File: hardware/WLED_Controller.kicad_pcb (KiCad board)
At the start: 2 copper layers, 50 x 57.5 mm, 79 parts, among them J1 Conn_01x01_Male, J11 Conn_01x01_Male, J12 Conn_01x01_Male, J2 USB_B_Micro, J3 Conn_01x01_Male, J4 Conn_01x01_Male, J5 Conn_01x01_Male, Q1 S8050_SMD, Q2 S8050_SMD, Q3 2N7002, Q4 2N7002, SW1 SW_SPST, SW2 SW_SPST, U1 AMS1117-3.3, U2 AMS1117-3.3, U3 TP4056, U4 ESP-12F, U5 CP2102N-A01-GQFN28, U6 AP2007, U7 AP2007, U8 AP2007

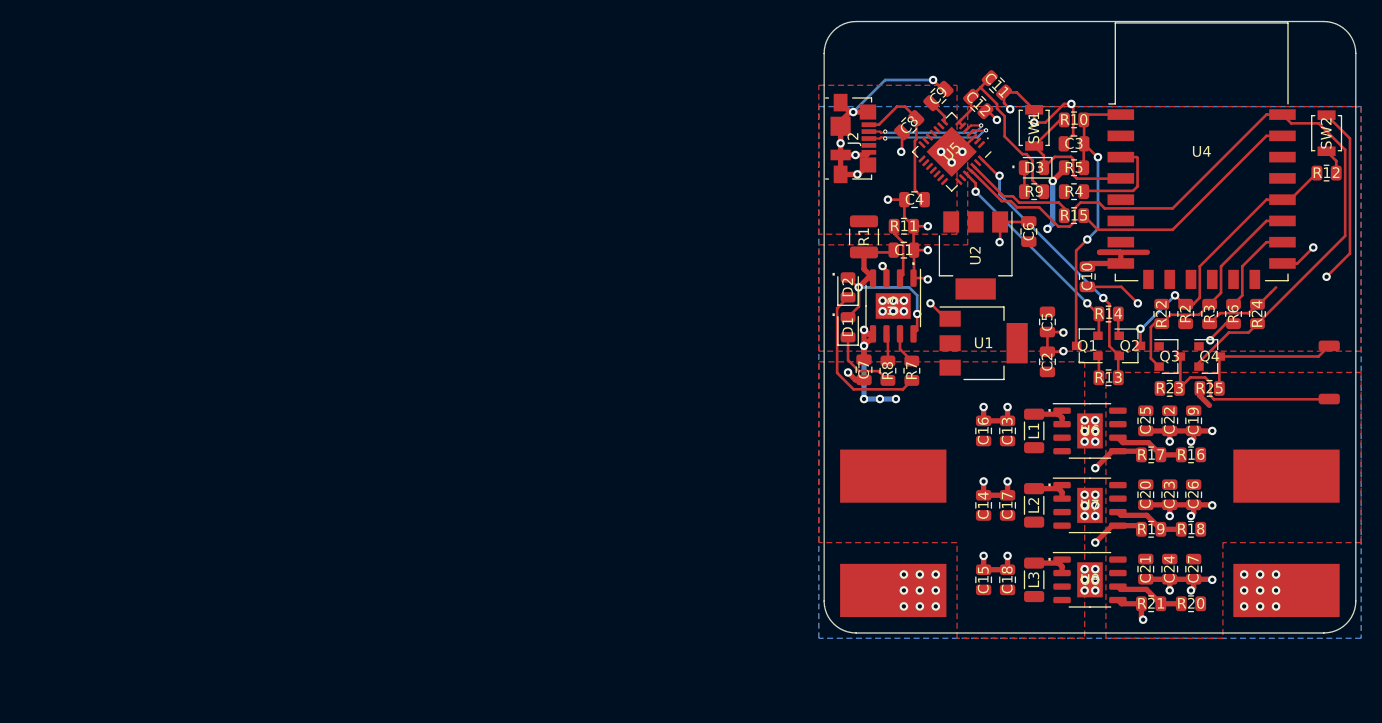
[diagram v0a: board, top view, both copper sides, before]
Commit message: Updated to v2.0.0
Contains the PCB design and fabrication files for v2.0.0 of the WLED
controller.
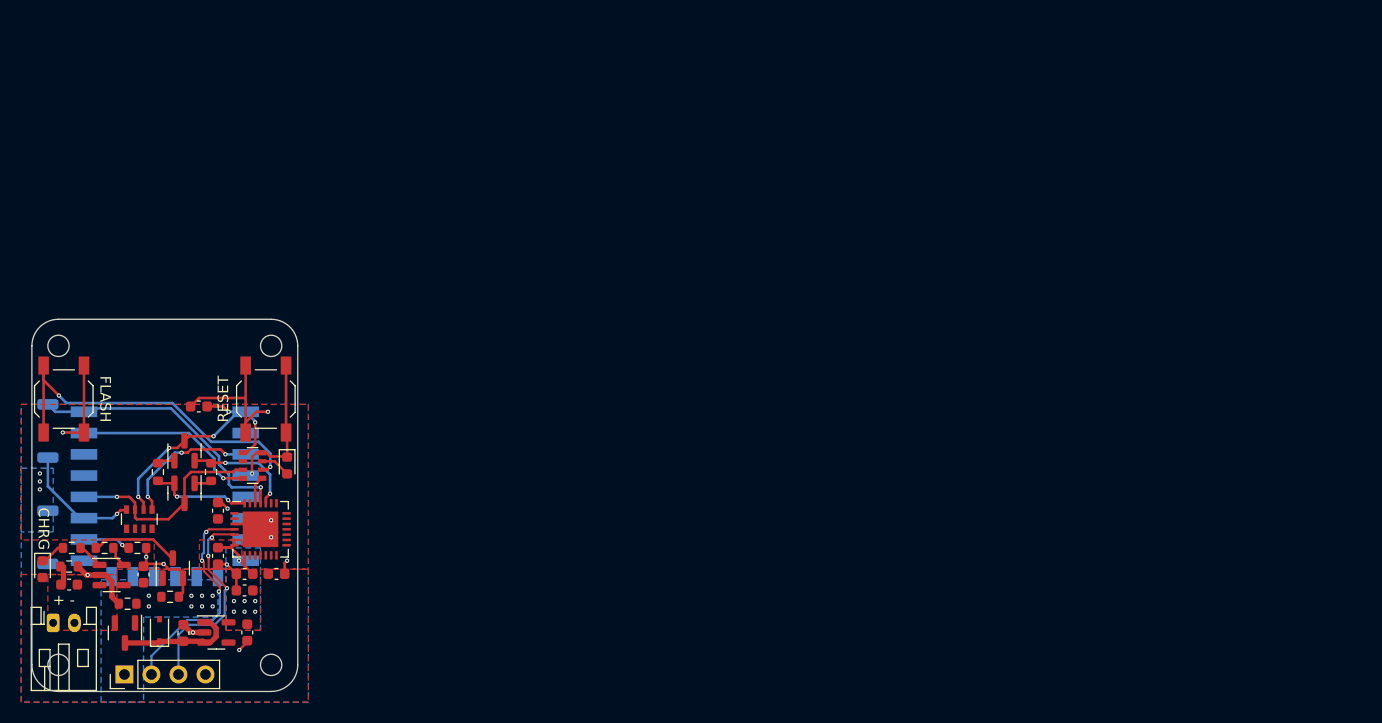
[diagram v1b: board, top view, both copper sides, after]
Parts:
- removed C11: 10uF, Capacitor_SMD:C_0805_2012Metric
- removed C12: 0.1uF, Capacitor_SMD:C_0805_2012Metric
- removed C13, C14, C15, C16, C17, C18, C19, C20, C21, C22, C23, C24, C25, C26, C27: 22u, Capacitor_SMD:C_0805_2012Metric
- removed J11, J12: Conn_01x01_Male, Connector_Wire:SolderWirePad_1x01_SMD_1x2mm
- removed L1, L2, L3: 3.3u, Inductor_SMD:L_1206_3216Metric
- removed R10, R12, R15, R9: 470, Resistor_SMD:R_0805_2012Metric
- removed R11: 1.2k, Resistor_SMD:R_0805_2012Metric
- removed R13, R14, R22, R23, R24, R25: 10k, Resistor_SMD:R_0805_2012Metric
- removed R16, R18, R20: 100k, Resistor_SMD:R_0805_2012Metric
- removed R17, R19, R21: 33k, Resistor_SMD:R_0805_2012Metric
- removed U5: CP2102N-A01-GQFN28, Package_DFN_QFN:QFN-28-1EP_5x5mm_P0.5mm_EP3.35x3.35mm
- removed U6, U7, U8: AP2007, myfootprints:SOP-8-EP_3.9x4.9mm_P1.27mm
- added J6: Conn_01x01_Male, Connector_Wire:SolderWirePad_1x01_SMD_1x2mm, B.Cu at (51.5, 118.0)
- added RN1: 10k, Resistor_SMD:R_Array_Convex_4x0603, F.Cu at (60.1, 113.8)
- added RN2: 470, Resistor_SMD:R_Array_Convex_4x0603, F.Cu at (70.8, 108.8)
- added kibuzzard-6350B1D2: G***, kibuzzard-6350B1D2, B.Cu at (62.5, 122.9)
- C1, C6, C8: value 10uF -> 0.1uF; footprint Capacitor_SMD:C_0805_2012Metric -> Capacitor_SMD:C_0603_1608Metric
- C10, C7: footprint Capacitor_SMD:C_0805_2012Metric -> Capacitor_SMD:C_0603_1608Metric
- C2, C4, C5: value 10uF -> 1uF; footprint Capacitor_SMD:C_0805_2012Metric -> Capacitor_SMD:C_0603_1608Metric
- C3: value 0.1uF -> 1uF; footprint Capacitor_SMD:C_0805_2012Metric -> Capacitor_SMD:C_0603_1608Metric
- C9: value 0.1uF -> 10uF; footprint Capacitor_SMD:C_0805_2012Metric -> Capacitor_SMD:C_0603_1608Metric
- D1: value LED -> 1N5819; footprint LED_SMD:LED_0805_2012Metric -> Diode_SMD:D_SOD-323
- D2, D3: footprint LED_SMD:LED_0805_2012Metric -> LED_SMD:LED_0603_1608Metric
- J1: value Conn_01x01_Male -> Conn_01x02_Male; footprint Connector_Wire:SolderWirePad_1x01_SMD_5x10mm -> Connector_JST:JST_PH_S2B-PH-K_1x02_P2.00mm_Horizontal
- J2: value USB_B_Micro -> Conn_01x04; footprint Connector_USB:USB_Micro-B_Molex_47346-0001 -> Connector_PinHeader_2.54mm:PinHeader_1x04_P2.54mm_Vertical
- J3, J4, J5: footprint Connector_Wire:SolderWirePad_1x01_SMD_5x10mm -> Connector_Wire:SolderWirePad_1x01_SMD_1x2mm; moved to B.Cu
- Q1: value S8050_SMD -> AO3401A
- Q2: value S8050_SMD -> AO3400A
- Q3, Q4: value 2N7002 -> AO3400A
- R1: value 0.4 -> 10k; footprint Resistor_SMD:R_1210_3225Metric -> Resistor_SMD:R_0603_1608Metric
- R2, R3: value 10k -> 100k; footprint Resistor_SMD:R_0805_2012Metric -> Resistor_SMD:R_0603_1608Metric
- R4: value 10k -> 330; footprint Resistor_SMD:R_0805_2012Metric -> Resistor_SMD:R_0603_1608Metric
- R5: value 10k -> 2k; footprint Resistor_SMD:R_0805_2012Metric -> Resistor_SMD:R_0603_1608Metric
- R6: value 10k -> 1; footprint Resistor_SMD:R_0805_2012Metric -> Resistor_SMD:R_0603_1608Metric
- R7, R8: value 1k -> 10k; footprint Resistor_SMD:R_0805_2012Metric -> Resistor_SMD:R_0603_1608Metric
- SW1, SW2: footprint Button_Switch_SMD:SW_SPST_B3U-1000P -> Button_Switch_SMD:SW_SPST_TL3342
- U1: value AMS1117-3.3 -> AP2112K-3.3; footprint Package_TO_SOT_SMD:SOT-223 -> Package_TO_SOT_SMD:SOT-23-5
- U2: value AMS1117-3.3 -> LTC4054ES5-4.2; footprint Package_TO_SOT_SMD:SOT-223 -> Package_TO_SOT_SMD:TSOT-23-5
- U3: value TP4056 -> ESP-12F; footprint myfootprints:SOP-8-EP_3.9x4.9mm_P1.27mm -> RF_Module:ESP-12E; moved to B.Cu
- U4: value ESP-12F -> CP2102N-Axx-xQFN28; footprint RF_Module:ESP-12E -> Package_DFN_QFN:QFN-28-1EP_5x5mm_P0.5mm_EP3.35x3.35mm
- moved SW2 121.4 mm to (53.0, 102.5)
- moved J5 117.8 mm to (51.5, 103.0), turned to 90 degrees
- moved J4 116.5 mm to (51.5, 108.0), turned to 90 degrees
- moved R6 112.0 mm to (53.5, 118.2), turned to 180 degrees
- moved R2 103.2 mm to (59.0, 121.8), turned to 180 degrees
- moved R3 101.3 mm to (63.0, 121.1), turned to 0 degrees
- moved D3 100.6 mm to (51.0, 118.5), turned to -90 degrees
- moved R4 100.0 mm to (53.8, 116.5), turned to 0 degrees
- moved R5 97.9 mm to (56.8, 116.5)
- moved Q4 97.3 mm to (64.3, 111.4), turned to -90 degrees
- moved U4 95.4 mm to (71.5, 114.8)
- moved C5 95.3 mm to (53.5, 120.0), turned to 0 degrees
- moved Q1 94.4 mm to (58.8, 124.5), turned to -90 degrees
- moved Q3 93.1 mm to (64.3, 107.4), turned to 90 degrees
- moved Q2 92.4 mm to (63.2, 118.4), turned to 90 degrees
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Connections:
- C1 pad 1: Net-(C1-Pad1) -> /nRST
- C10 pad 1: GND -> +3V3
- C10 pad 2: +3V3 -> GND
- C2 pad 1: +BATT -> Net-(C2-Pad1)
- C3 pad 1: /nRST -> +3V3
- C5 pad 1: +3V3 -> Net-(C5-Pad1)
- C5 pad 2: GND -> +BATT
- C6 pad 1: +3V3 -> GND
- C6 pad 2: GND -> +3V3
- C7 pad 1: +BATT -> VBUS
- C9 pad 1: VBUS -> +3V3
- D1 pad 1: Net-(D1-Pad1) -> Net-(C2-Pad1)
- D1 pad 2: Net-(C1-Pad1) -> VBUS
- D2 pad 1: Net-(D2-Pad1) -> /GPIO16
- D2 pad 2: Net-(C1-Pad1) -> Net-(D2-Pad2)
- D3 pad 1: /GPIO16 -> Net-(D3-Pad1)
- D3 pad 2: Net-(D3-Pad2) -> VBUS
- J2 pad 2: /D_N -> /D_P
- J2 pad 3: /D_P -> /D_N
- J2 pad 4: unconnected-(J2-Pad4) -> GND
- J3 pad 1: GND -> +3V3
- J4 pad 1: +5V -> /GPIO2
- J5 pad 1: GND -> /RXI
- Q1 pad 1: Net-(Q1-Pad1) -> VBUS
- Q1 pad 2: /RTS -> +BATT
- Q1 pad 3: /nRST -> Net-(C2-Pad1)
- Q2 pad 1: Net-(Q2-Pad1) -> VBUS
- Q2 pad 2: /DTR -> GND
- Q2 pad 3: /GPIO0 -> Net-(Q2-Pad3)
- Q3 pad 1: +3V3 -> Net-(Q3-Pad1)
- Q3 pad 2: /GPIO2 -> /RTS
- Q3 pad 3: /DATA -> /nRST
- Q4 pad 1: +3V3 -> Net-(Q4-Pad1)
- Q4 pad 2: /TXD -> /DTR
- Q4 pad 3: /CLOCK -> /GPIO0
- R1 pad 1: Net-(C1-Pad1) -> /GPIO15
- R1 pad 2: VBUS -> GND
- R2 pad 1: /GPIO0 -> VBUS
- R2 pad 2: +3V3 -> GND
- R3 pad 1: /GPIO2 -> VBUS
- R3 pad 2: +3V3 -> GND
- R4 pad 1: /EN -> Net-(D3-Pad1)
- R4 pad 2: +3V3 -> Net-(R4-Pad2)
- R5 pad 1: /nRST -> Net-(R5-Pad1)
- R5 pad 2: +3V3 -> Net-(Q2-Pad3)
- R6 pad 1: /GPIO15 -> GND
- R6 pad 2: GND -> Net-(C5-Pad1)
- R7 pad 1: Net-(R7-Pad1) -> Net-(Q3-Pad1)
- R7 pad 2: Net-(D2-Pad1) -> /DTR
- R8 pad 1: Net-(R8-Pad1) -> Net-(Q4-Pad1)
- R8 pad 2: Net-(D1-Pad1) -> /RTS
- U1 pad 1: GND -> Net-(C2-Pad1)
- U1 pad 2: +3V3 -> GND
- U1 pad 3: +BATT -> Net-(C2-Pad1)
- U1 pad 4: (no net) -> unconnected-(U1-Pad4)
- U2 pad 1: GND -> Net-(R4-Pad2)
- U2 pad 2: +3V3 -> GND
- U2 pad 3: VBUS -> +BATT
- U2 pad 4: (no net) -> VBUS
- U3 pad 1: GND -> /nRST
- U3 pad 2: Net-(R11-Pad1) -> unconnected-(U3-Pad2)
- U3 pad 3: GND -> /EN
- U3 pad 4: Net-(C1-Pad1) -> /GPIO16
- U3 pad 5: +BATT -> /SCLK
- U3 pad 6: Net-(R8-Pad1) -> /MISO
- U3 pad 7: Net-(R7-Pad1) -> /MOSI
- U3 pad 8: Net-(C1-Pad1) -> +3V3
- U4 pad 1: /nRST -> unconnected-(U4-Pad1)
- U4 pad 15: GND -> unconnected-(U4-Pad15)
- U4 pad 16: /GPIO15 -> unconnected-(U4-Pad16)
- U4 pad 17: /GPIO2 -> unconnected-(U4-Pad17)
- U4 pad 18: /GPIO0 -> unconnected-(U4-Pad18)
- U4 pad 19: /SDA -> unconnected-(U4-Pad19)
- U4 pad 20: /SCL -> unconnected-(U4-Pad20)
- U4 pad 21: /RXD -> unconnected-(U4-Pad21)
- U4 pad 22: /TXD -> unconnected-(U4-Pad22)
- U4 pad 3: /EN -> GND
- U4 pad 4: /GPIO16 -> /D_P
- U4 pad 5: /SCLK -> /D_N
- U4 pad 6: /MISO -> +3V3
- U4 pad 7: /MOSI -> +3V3
- U4 pad 8: +3V3 -> VBUS
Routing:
- net GND: track 157.3 -> 50.4 mm, vias 87 -> 12
- net /TXD: track 71.5 -> 0.00 mm
- net +3V3: track 43.2 -> 4.92 mm, vias 2 -> 10
- net Net-(RN2-Pad6): track 2.43 -> 34.0 mm, vias 0 -> 2
- net /RXI: track 0.00 -> 25.6 mm, vias 0 -> 1
- net /RXD: track 22.9 -> 0.00 mm
- net Net-(C1-Pad1): track 21.5 -> 0.00 mm, vias 2 -> 0
- net /DATA: track 19.1 -> 0.00 mm
- net /TXO: track 0.00 -> 17.4 mm, vias 0 -> 1
- net /DTR: track 26.1 -> 9.65 mm
- net Net-(D2-Pad1): track 15.5 -> 0.00 mm
- net VBUS: track 16.0 -> 2.07 mm, vias 0 -> 8
- net /CLOCK: track 13.7 -> 0.00 mm
- net +BATT: track 13.3 -> 0.00 mm, vias 5 -> 0
- net Net-(C2-Pad1): track 0.00 -> 11.1 mm
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- added copper zone on B.Cu, net +3V3
- added copper zone on B.Cu, net VBUS
- removed copper zone on F.Cu, net +5V
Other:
- board size 50 x 57.5 mm -> 25 x 35 mm
- rule pad_to_mask_clearance: 0 -> 0.05
- board text added: "+ -"
- board text added: "- +"
- board text added: "3V3"
- board text added: "CHRG"
- board text added: "CLK"
- board text added: "DT"
- board text added: "Designed by Shadman Habib"
- board text added: "FLASH"
- board text added: "GND"
- board text added: "GND D- D+ 5V"
- board text added: "RESET"
- board text removed: "."
